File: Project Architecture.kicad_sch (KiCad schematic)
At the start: 32 parts, among them J1 Screw_Terminal_01x04, U1 TMP102xxDRL

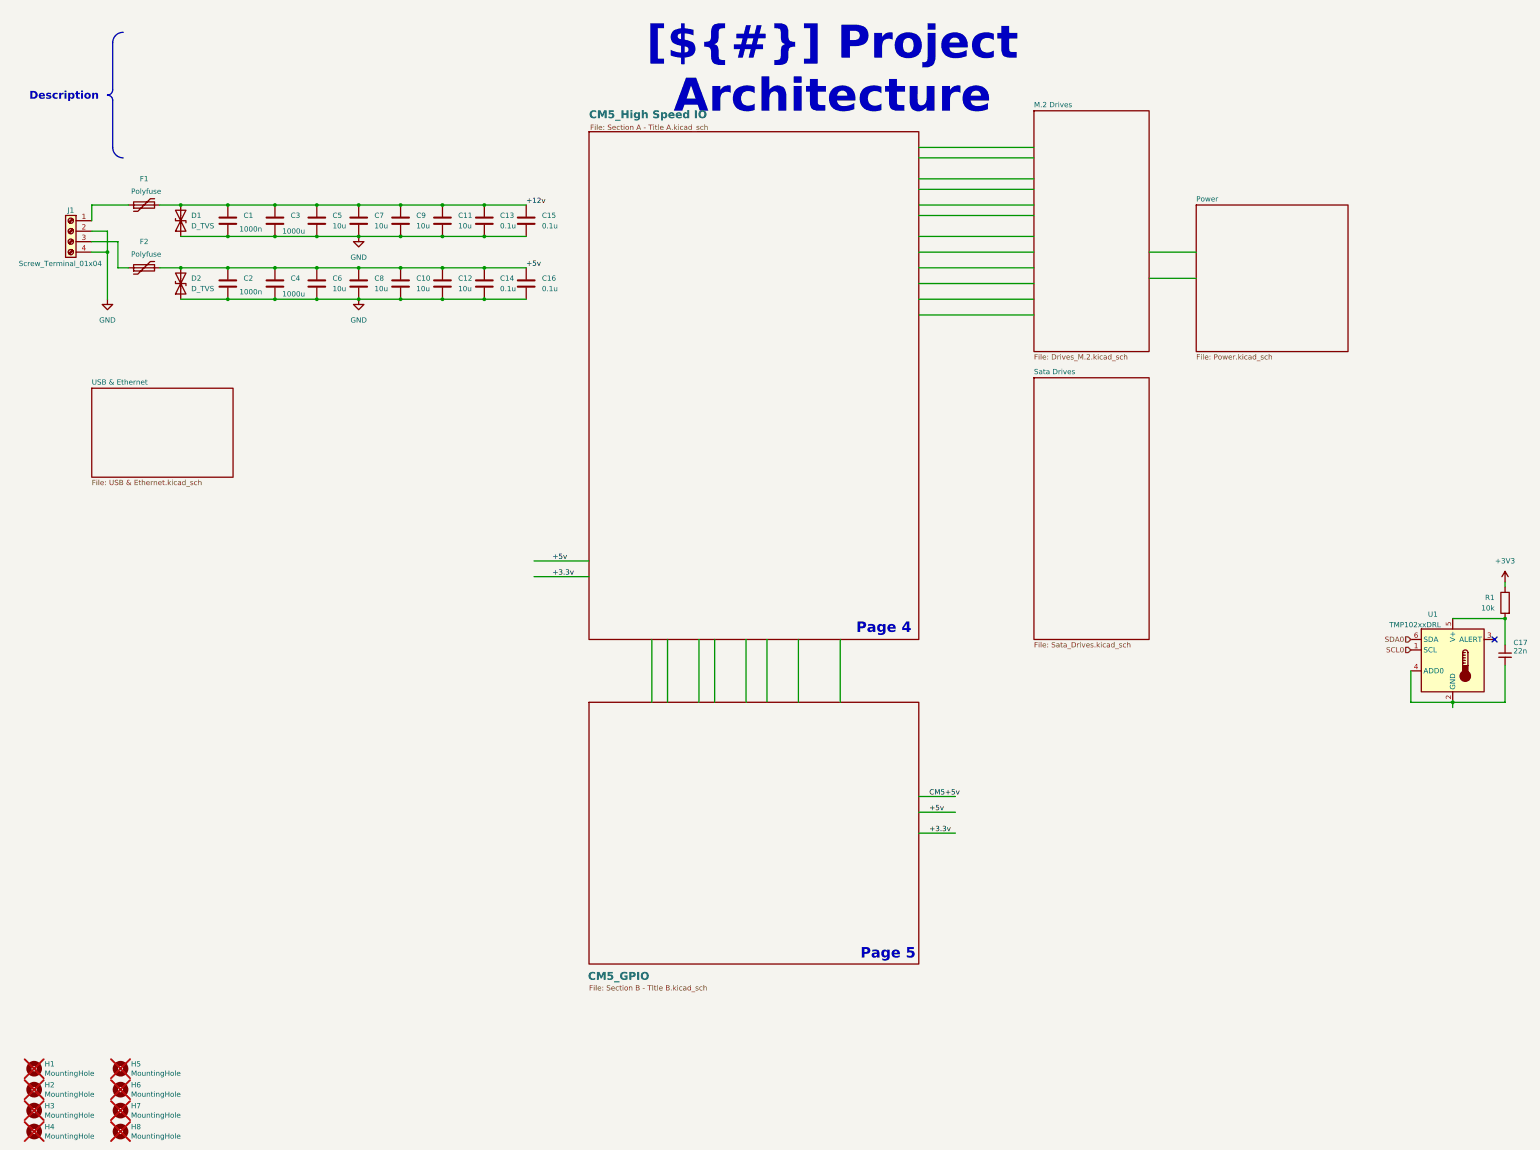
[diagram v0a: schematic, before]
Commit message: Swiitched to JSM561
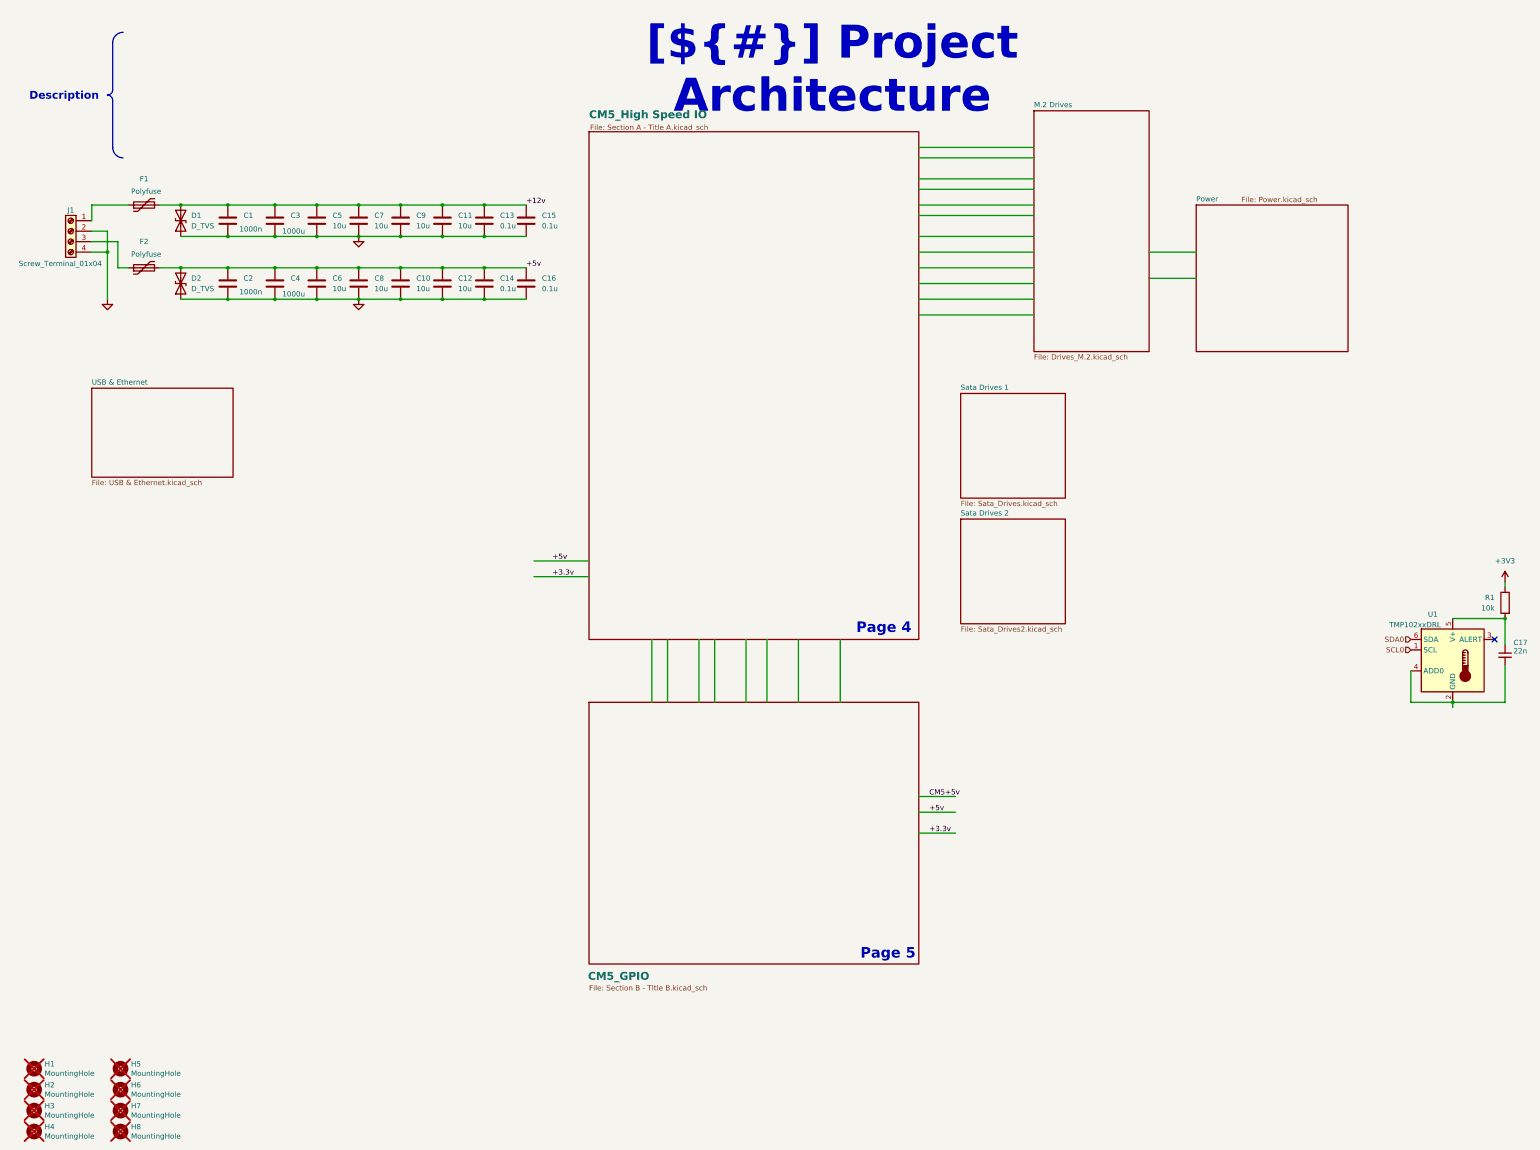
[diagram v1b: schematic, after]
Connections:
- removed net GND: C1.2, C10.2, C11.2, C12.2, C13.2, C14.2, C15.2, C16.2, C2.2, C3.2, C4.2, C5.2, C6.2, C7.2, C8.2, C9.2, D1.1 (A1), D2.1 (A1), J1.2 (Pin_2), J1.4 (Pin_4)
- new net: C1.2, C11.2, C13.2, C15.2, C3.2, C5.2, C7.2, C9.2, D1.1 (A1)
- new net: C10.2, C12.2, C14.2, C16.2, C2.2, C4.2, C6.2, C8.2, D2.1 (A1)
- new net: J1.2 (Pin_2), J1.4 (Pin_4)
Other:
- sheet Sata Drives renamed Sata Drives 1
- added sheet Sata Drives 2 (Sata_Drives2.kicad_sch)
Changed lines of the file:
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@@
 			)
 		)
-		(property "Value" "GND"
+		(property "Value" "~"
 			(at 95.25 68.58 0)
 			(effects
@@
 			)
 		)
-		(property "Value" "GND"
+		(property "Value" "~"
 			(at 95.25 83.82 0)
 			(effects
@@
 			)
 		)
-		(property "Value" "GND"
+		(property "Value" "~"
 			(at 34.29 83.82 0)
 			(effects
@@
 	)
 	(sheet
-		(at 298.45 55.88)
-		(size 36.83 35.56)
+		(at 241.3 132.08)
+		(size 25.4 25.4)
 		(exclude_from_sim no)
 		(in_bom yes)
@@
 			(width 0.1524)
 			(type solid)
+			(color 168 218 255 1)
+		)
+		(fill
+			(color 177 187 255 1.0000)
+		)
+		(property "Sheetname" "Sata Drives 2"
+			(at 241.3 131.3684 0)
+			(effects
+				(font
+					(size 1.27 1.27)
+				)
+				(justify left bottom)
+			)
+		)
+		(property "Sheetfile" "Sata_Drives2.kicad_sch"
+			(at 241.3 158.0646 0)
+			(effects
+				(font
+					(size 1.27 1.27)
+				)
+				(justify left top)
+			)
+		)
+		(instances
+			(project "CM5 Nas"
+				(path "/0650c7a8-acba-429c-9f8e-eec0baf0bc1c/fede4c36-00cc-4d3d-b71c-5243ba232202"
+					(page "9")
+				)
+			)
+		)
+	)
+	(sheet
+		(at 298.45 55.88)
+		(size 36.83 35.56)
+		(exclude_from_sim no)
+		(in_bom yes)
+		(on_board yes)
+		(dnp no)
+		(stroke
+			(width 0.1524)
+			(type solid)
 		)
 		(fill
@@
 		)
 		(property "Sheetfile" "Power.kicad_sch"
-			(at 298.45 92.0246 0)
+			(at 309.372 53.848 0)
 			(effects
 				(font
@@
 	)
 	(sheet
-		(at 259.08 97.79)
-		(size 27.94 63.5)
+		(at 241.3 101.6)
+		(size 25.4 25.4)
 		(exclude_from_sim no)
 		(in_bom yes)
@@
 			(color 168 218 255 1.0000)
 		)
-		(property "Sheetname" "Sata Drives"
-			(at 259.08 97.0784 0)
+		(property "Sheetname" "Sata Drives 1"
+			(at 241.3 100.8884 0)
 			(effects
 				(font
@@
 		)
 		(property "Sheetfile" "Sata_Drives.kicad_sch"
-			(at 259.08 161.8746 0)
-			(effects
-				(font
+			(at 241.3 127.5846 0)
+			(effects
+				(font

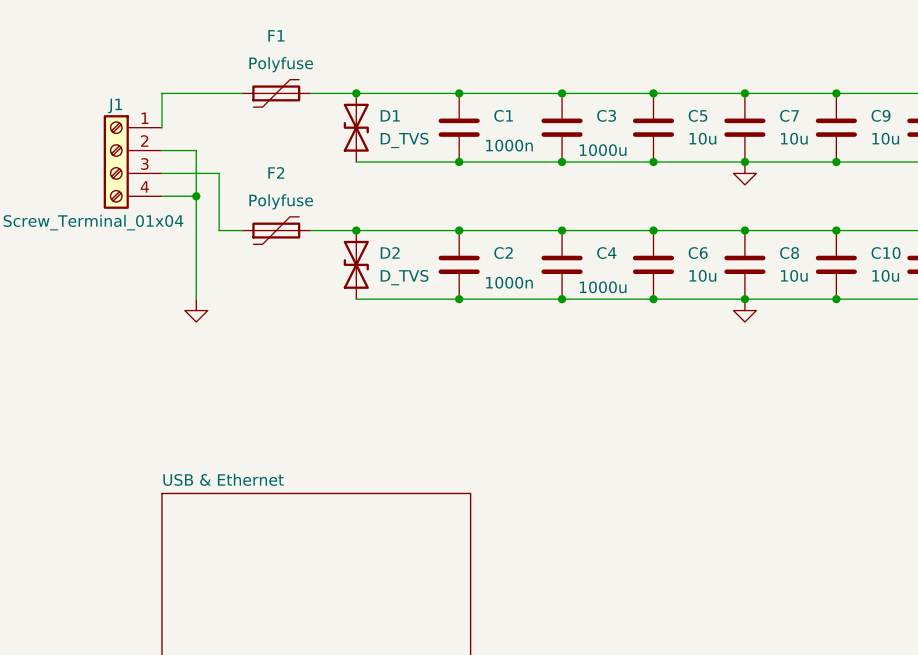
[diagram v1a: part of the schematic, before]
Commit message: Removed Ethernet
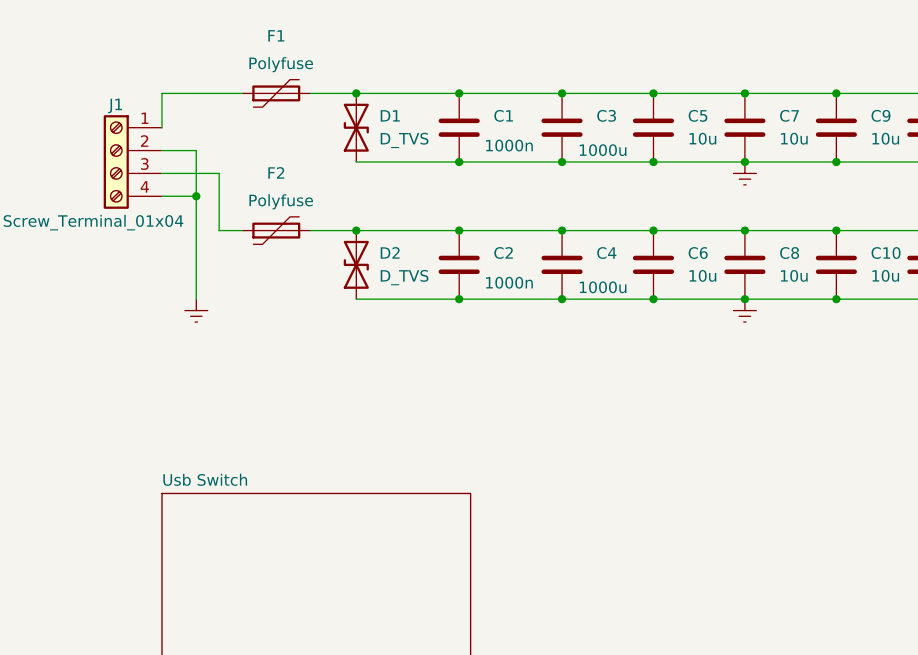
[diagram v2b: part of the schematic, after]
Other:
- sheet USB & Ethernet renamed Usb Switch
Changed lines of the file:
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@@
 	)
 	(symbol
-		(lib_id "power:GND")
+		(lib_id "power:Earth")
 		(at 95.25 63.5 0)
 		(unit 1)
@@
 		)
 		(property "Value" "~"
-			(at 95.25 68.58 0)
-			(effects
-				(font
-					(size 1.27 1.27)
-				)
+			(at 97.79 64.77 0)
+			(effects
+				(font
+					(size 1.27 1.27)
+				)
+				(justify left)
 			)
 		)
@@
 			)
 		)
-		(property "Datasheet" ""
+		(property "Datasheet" "~"
 			(at 95.25 63.5 0)
 			(effects
@@
 			)
 		)
-		(property "Description" "Power symbol creates a global label with name \"GND\" , ground"
+		(property "Description" "Power symbol creates a global label with name \"Earth\""
 			(at 95.25 63.5 0)
 			(effects
@@
 	)
 	(symbol
-		(lib_id "power:GND")
+		(lib_id "power:Earth")
 		(at 95.25 78.74 0)
 		(unit 1)
@@
 		)
 		(property "Value" "~"
-			(at 95.25 83.82 0)
-			(effects
-				(font
-					(size 1.27 1.27)
-				)
+			(at 97.79 80.01 0)
+			(effects
+				(font
+					(size 1.27 1.27)
+				)
+				(justify left)
 			)
 		)
@@
 			)
 		)
-		(property "Datasheet" ""
+		(property "Datasheet" "~"
 			(at 95.25 78.74 0)
 			(effects
@@
 			)
 		)
-		(property "Description" "Power symbol creates a global label with name \"GND\" , ground"
+		(property "Description" "Power symbol creates a global label with name \"Earth\""
 			(at 95.25 78.74 0)
 			(effects
@@
 	)
 	(symbol
-		(lib_id "power:GND")
+		(lib_id "power:Earth")
 		(at 34.29 78.74 0)
 		(unit 1)
@@
 		)
 		(property "Value" "~"
-			(at 34.29 83.82 0)
-			(effects
-				(font
-					(size 1.27 1.27)
-				)
+			(at 36.83 80.01 0)
+			(effects
+				(font
+					(size 1.27 1.27)
+				)
+				(justify left)
 			)
 		)
@@
 			)
 		)
-		(property "Datasheet" ""
+		(property "Datasheet" "~"
 			(at 34.29 78.74 0)
 			(effects
@@
 			)
 		)
-		(property "Description" "Power symbol creates a global label with name \"GND\" , ground"
+		(property "Description" "Power symbol creates a global label with name \"Earth\""
 			(at 34.29 78.74 0)
 			(effects
@@
 			(color 0 0 0 0.0000)
 		)
-		(property "Sheetname" "USB & Ethernet"
+		(property "Sheetname" "Usb Switch"
 			(at 30.48 99.6184 0)
 			(effects

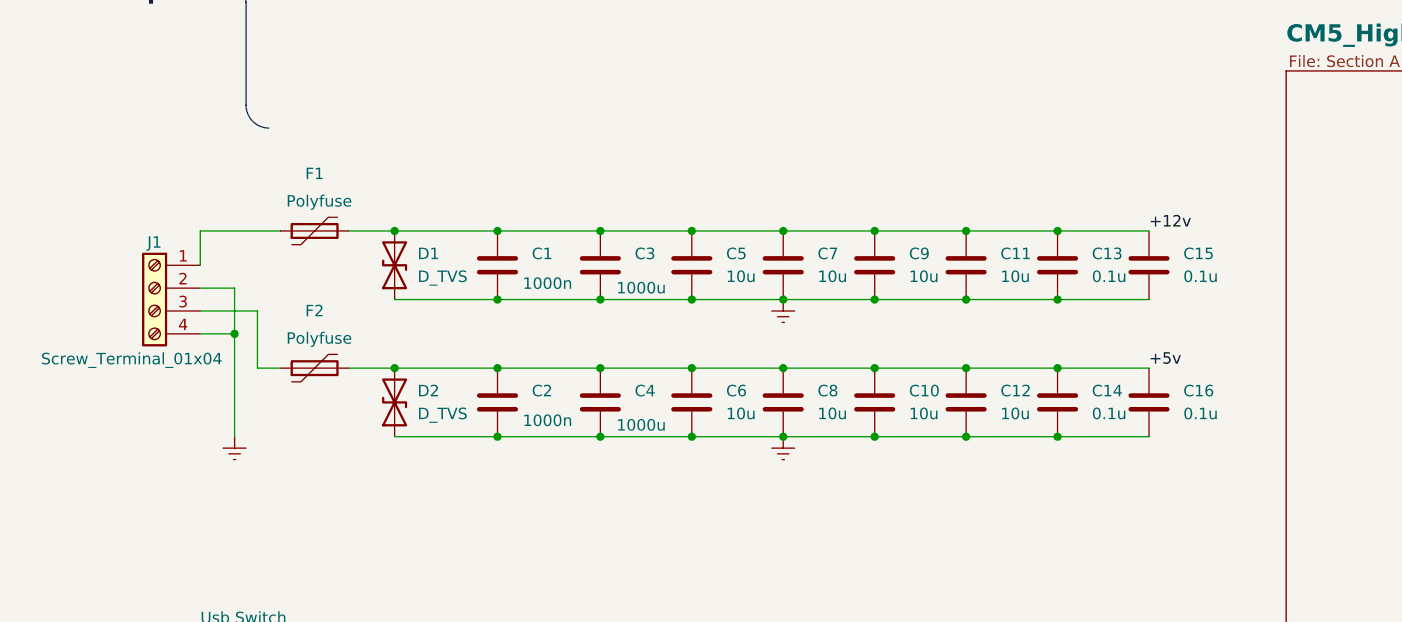
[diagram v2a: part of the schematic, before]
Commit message: More Fans
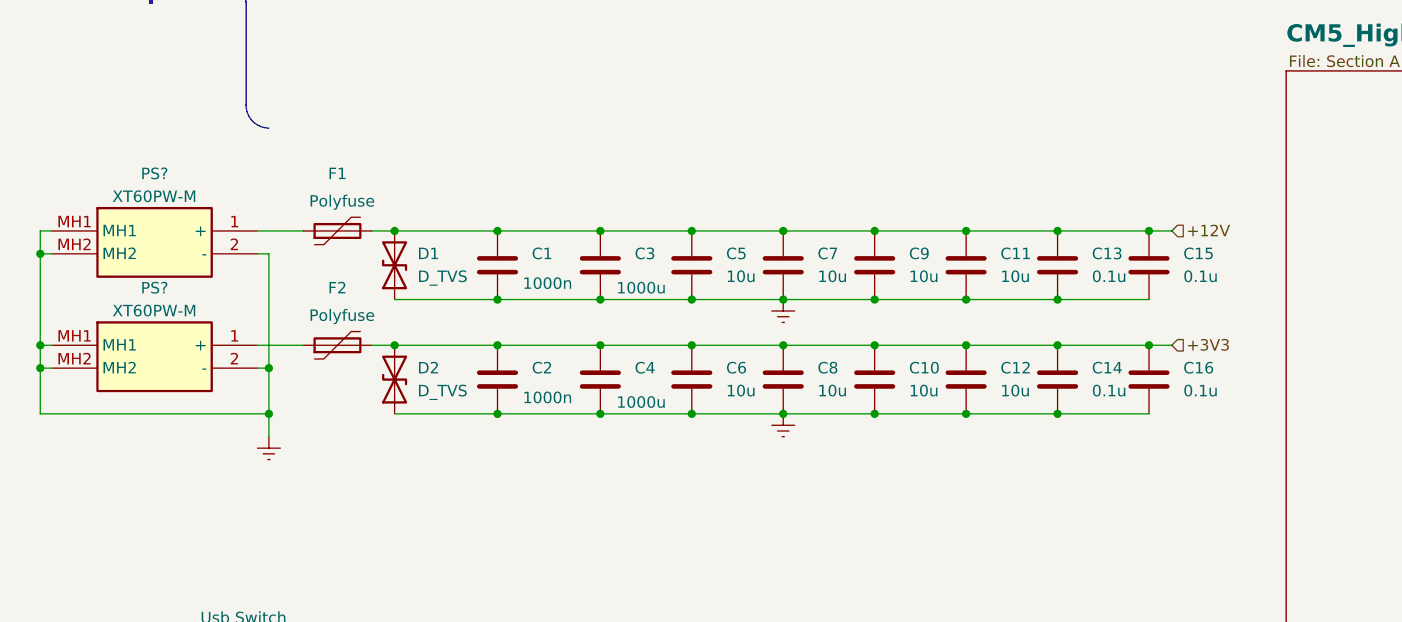
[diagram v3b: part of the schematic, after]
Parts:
- removed J1: Screw_Terminal_01x04, symbol Connector:Screw_Terminal_01x04
- added PS? (x2): XT60PW-M, XT60PWM, symbol XT60PW-M:XT60PW-M
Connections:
- net +3V3: now also C10.1, C12.1, C14.1, C16.1, C2.1, C4.1, C6.1, C8.1, D2.2 (A2), F2.2
- net +5v: no longer C10.1, C12.1, C14.1, C16.1, C2.1, C4.1, C6.1, C8.1, D2.2 (A2), F2.2
- net at F1.1: now also PS?.1 (+)
- net at F2.1: now also PS?.1 (+)
- net +12v renamed +12V
- new net: PS?.2 (-), PS?.2 (-), PS?.MH1, PS?.MH1, PS?.MH2, PS?.MH2
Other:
- moved on the sheet: C10, C12, C14, C16, C2, C4, C6, C8, D2, F1, F2
